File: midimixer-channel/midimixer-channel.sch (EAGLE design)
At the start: 110 parts, among them IC1 74LS595D, IC2 74LS595D, IC3 74LS595D, IC4 74165D, IC5 74165D, U1 LM1117IMPX-3.3/NOPB, Y1 8MHz 695-HCM49-8-U

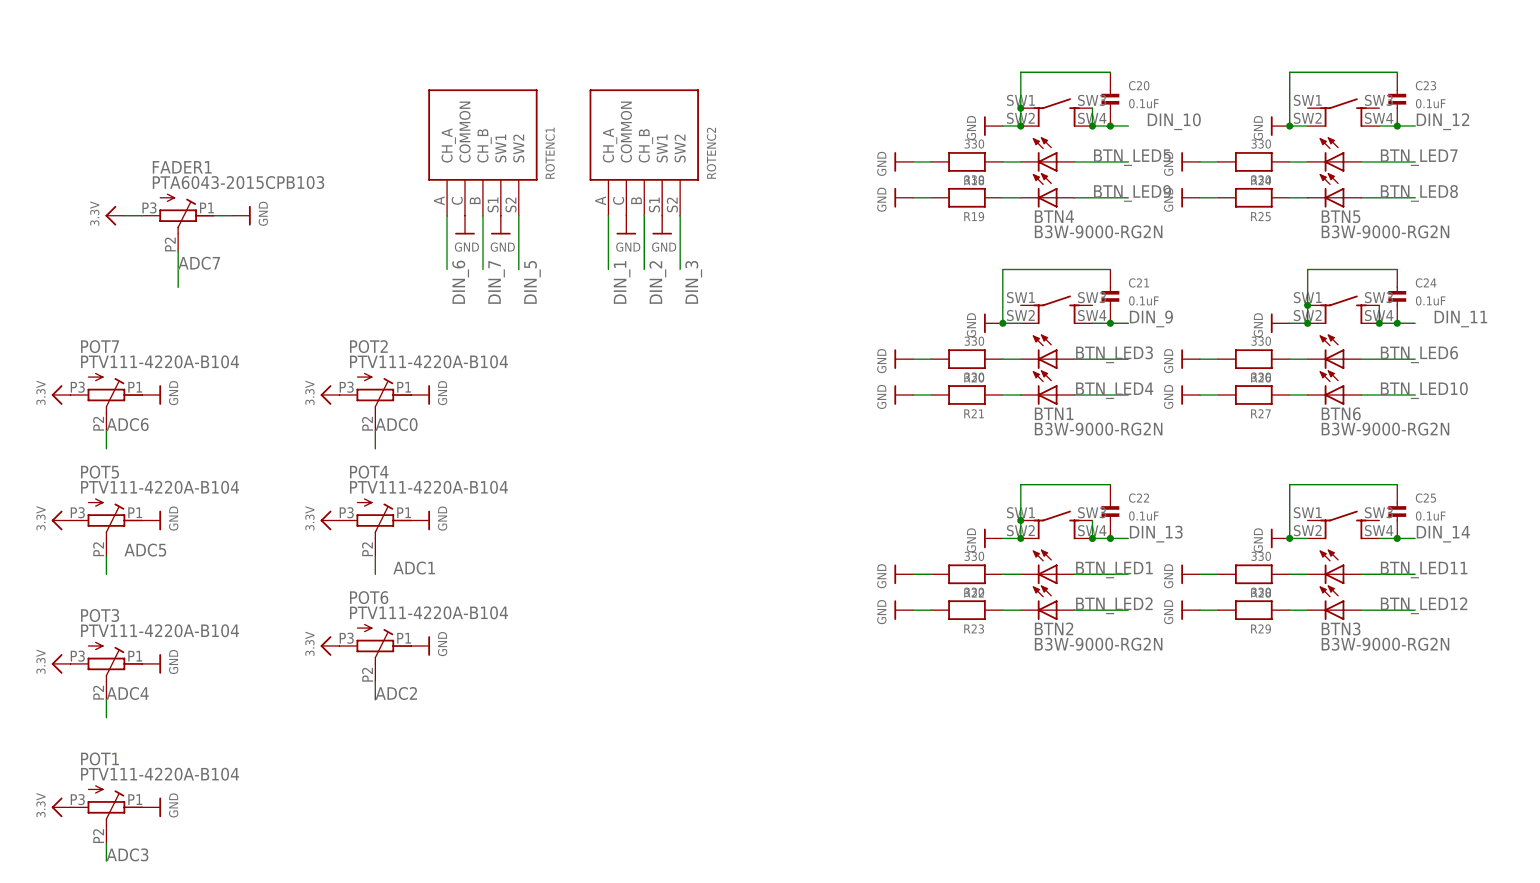
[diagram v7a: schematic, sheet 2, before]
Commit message: midimixer-channel: switch pots to available ones, switch ssd1306 to 7 pin
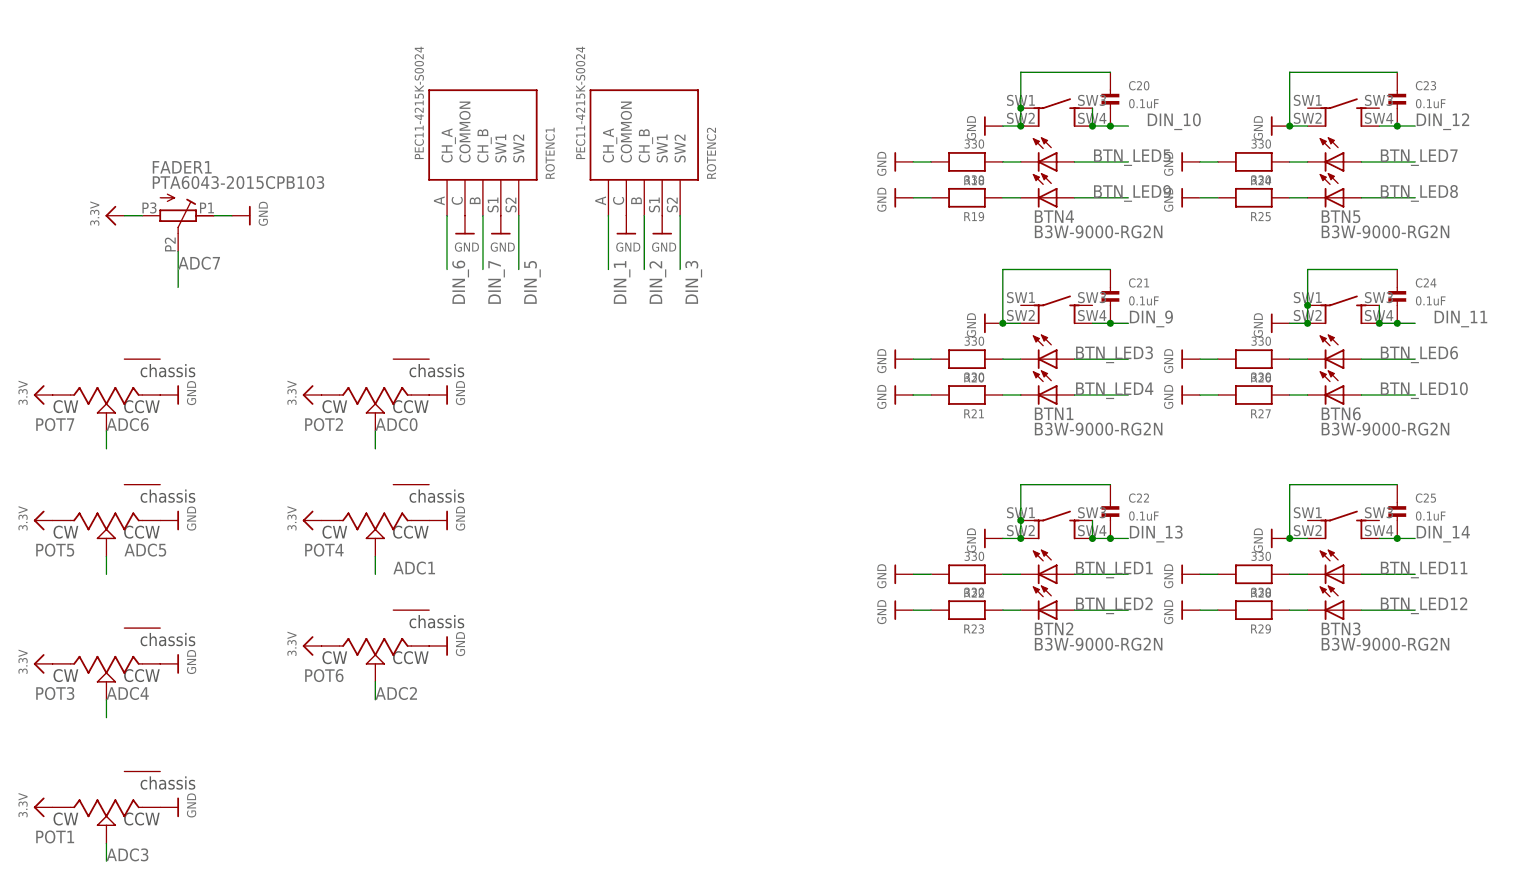
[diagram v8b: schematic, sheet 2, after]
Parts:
- removed LCD1: SSD1306-ALI, keves:SSD1306-ALI
- added LCD: SSD1306-7PIN, keves:SSD1306-7PIN
- POT1, POT2, POT3, POT4, POT5, POT6, POT7: value PTV111-4220A-B104 -> (none); device keves:PTV111-4220A-B104 -> keves:POTENTIOMETERPTV09A_VERTICAL
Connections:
- new net LCD_RST: CPU1.PC4, LCD.RST
- net 3.3V: now also LCD.VCC, POT1.CW, POT2.CW, POT3.CW, POT4.CW, POT5.CW, POT6.CW, POT7.CW; no longer LCD1.VCC, POT1.E, POT2.E, POT3.E, POT4.E, POT5.E, POT6.E, POT7.E
- net ADC0: now also POT2.WIPER; no longer POT2.S
- net ADC1: now also POT4.WIPER; no longer POT4.S
- net ADC2: now also POT6.WIPER; no longer POT6.S
- net ADC3: now also POT1.WIPER; no longer POT1.S
- net ADC4: now also POT3.WIPER; no longer POT3.S
- net ADC5: now also POT5.WIPER; no longer POT5.S
- net ADC6: now also POT7.WIPER; no longer POT7.S
- net GND: now also LCD.GND, POT1.CCW, POT2.CCW, POT3.CCW, POT4.CCW, POT5.CCW, POT6.CCW, POT7.CCW; no longer LCD1.GND, POT1.A, POT2.A, POT3.A, POT4.A, POT5.A, POT6.A, POT7.A
- net LCD_CLK: now also LCD.CLK; no longer LCD1.CLK
- net LCD_CS: now also LCD.CS; no longer LCD1.CS
- net LCD_DC: now also LCD.DC; no longer LCD1.DC
- net LCD_MOSI: now also LCD.MOSI; no longer LCD1.MOSI
